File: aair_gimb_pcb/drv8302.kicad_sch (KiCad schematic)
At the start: 48 parts, among them U1 DRV8302, U3 TC2117

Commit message: pcb
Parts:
- D3: footprint Diode_SMD:D_SMA_Handsoldering -> Diode_SMD:D_SMA
- L1: footprint Inductor_SMD_Wurth:L_Wurth_WE-LQSH-2010 -> Inductor_SMD:L_7.3x7.3_H4.5
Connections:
- net GND: no longer C25.2, C26.2, C27.2, C31.1, C32.1, C33.1, C34.1, C35.1, C36.1, U1.29 (PVDD1)
- net H1_VS: now also R21.2
- net H2_VS: now also R22.2
- net H3_VS: now also R23.2
- net V_SUPPLY: now reaches C17.2, U1.53 (PVDD2), U1.54 (PVDD2)
- net V_SUPPLY: now also C25.2, C26.2, C27.2, C31.1, C32.1, C33.1, C34.1, C35.1, C36.1, U1.29 (PVDD1)
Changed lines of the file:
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@@
 	)
 	(junction
-		(at 85.09 69.85)
+		(at 162.56 68.58)
 		(diameter 0)
 		(color 0 0 0 0)
 	)
 	(junction
-		(at 157.48 144.78)
+		(at 85.09 69.85)
 		(diameter 0)
 		(color 0 0 0 0)
 	)
 	(junction
-		(at 158.75 129.54)
+		(at 157.48 144.78)
 		(diameter 0)
 		(color 0 0 0 0)
 	)
 	(junction
-		(at 177.8 68.58)
+		(at 158.75 129.54)
 		(diameter 0)
 		(color 0 0 0 0)
@@
 	)
 	(junction
-		(at 149.86 41.91)
-		(diameter 0)
-		(color 0 0 0 0)
-	)
-	(junction
 		(at 170.18 87.63)
 		(diameter 0)
@@
 	(wire
 		(pts
+			(xy 257.81 120.65) (xy 267.97 120.65)
+		)
+		(stroke
+			(width 0)
+			(type default)
+		)
+	)
+	(wire
+		(pts
 			(xy 85.09 69.85) (xy 110.49 69.85)
 		)
@@
 	(wire
 		(pts
-			(xy 154.94 68.58) (xy 166.37 68.58)
+			(xy 154.94 68.58) (xy 162.56 68.58)
 		)
 		(stroke
@@
 	(wire
 		(pts
+			(xy 162.56 60.96) (xy 162.56 68.58)
+		)
+		(stroke
+			(width 0)
+			(type default)
+		)
+	)
+	(wire
+		(pts
 			(xy 96.52 46.99) (xy 92.71 46.99)
 		)
@@
 	(wire
 		(pts
-			(xy 177.8 68.58) (xy 180.34 68.58)
+			(xy 171.45 68.58) (xy 180.34 68.58)
 		)
 		(stroke
@@
 	(wire
 		(pts
+			(xy 162.56 68.58) (xy 166.37 68.58)
+		)
+		(stroke
+			(width 0)
+			(type default)
+		)
+	)
+	(wire
+		(pts
 			(xy 83.82 129.54) (xy 83.82 140.97)
 		)
@@
 	(wire
 		(pts
-			(xy 90.17 26.67) (xy 90.17 30.48)
-		)
-		(stroke
-			(width 0)
-			(type default)
-		)
-	)
-	(wire
-		(pts
 			(xy 246.38 135.89) (xy 252.73 135.89)
 		)
@@
 	(wire
 		(pts
-			(xy 134.62 41.91) (xy 149.86 41.91)
-		)
-		(stroke
-			(width 0)
-			(type default)
-		)
-	)
-	(wire
-		(pts
 			(xy 96.52 44.45) (xy 121.92 44.45)
 		)
@@
 	(wire
 		(pts
-			(xy 149.86 41.91) (xy 149.86 43.18)
+			(xy 149.86 40.64) (xy 149.86 43.18)
 		)
 		(stroke
@@
 	(wire
 		(pts
+			(xy 177.8 60.96) (xy 162.56 60.96)
+		)
+		(stroke
+			(width 0)
+			(type default)
+		)
+	)
+	(wire
+		(pts
 			(xy 154.94 139.7) (xy 157.48 139.7)
 		)
@@
 	(wire
 		(pts
-			(xy 196.85 74.93) (xy 196.85 76.2)
+			(xy 269.24 132.08) (xy 257.81 132.08)
 		)
 		(stroke
@@
 	(wire
 		(pts
-			(xy 158.75 123.19) (xy 170.18 123.19)
+			(xy 196.85 74.93) (xy 196.85 76.2)
 		)
 		(stroke
@@
 	(wire
 		(pts
-			(xy 116.84 57.15) (xy 121.92 57.15)
+			(xy 158.75 123.19) (xy 170.18 123.19)
 		)
 		(stroke
@@
 	(wire
 		(pts
-			(xy 109.22 140.97) (xy 104.14 140.97)
+			(xy 116.84 57.15) (xy 121.92 57.15)
 		)
 		(stroke
@@
 	(wire
 		(pts
-			(xy 130.81 143.51) (xy 130.81 144.78)
+			(xy 109.22 140.97) (xy 104.14 140.97)
 		)
 		(stroke
@@
 	(wire
 		(pts
-			(xy 149.86 40.64) (xy 149.86 41.91)
+			(xy 130.81 143.51) (xy 130.81 144.78)
 		)
 		(stroke
@@
 	(wire
 		(pts
-			(xy 177.8 60.96) (xy 177.8 68.58)
+			(xy 257.81 107.95) (xy 267.97 107.95)
 		)
 		(stroke
@@
 	(wire
 		(pts
-			(xy 90.17 30.48) (xy 85.09 30.48)
-		)
-		(stroke
-			(width 0)
-			(type default)
-		)
-	)
-	(wire
-		(pts
 			(xy 92.71 46.99) (xy 92.71 54.61)
 		)
@@
 	(wire
 		(pts
-			(xy 171.45 68.58) (xy 177.8 68.58)
-		)
-		(stroke
-			(width 0)
-			(type default)
-		)
-	)
-	(wire
-		(pts
 			(xy 267.97 59.69) (xy 267.97 54.61)
 		)
@@
 	(global_label "V_SUPPLY"
 		(shape input)
-		(at 85.09 30.48 180)
-		(fields_autoplaced yes)
-		(effects
-			(font
-				(size 1.27 1.27)
-			)
-			(justify right)
-		)
-		(property "Intersheetrefs" "${INTERSHEET_REFS}"
-			(at 72.8519 30.48 0)
-			(effects
-				(font
-					(size 1.27 1.27)
-				)
-				(justify right)
-				(hide yes)
-			)
-		)
-	)
-	(global_label "V_SUPPLY"
-		(shape input)
 		(at 158.75 139.7 0)
 		(fields_autoplaced yes)
@@
 		)
 	)
+	(hierarchical_label "H2_VS"
+		(shape input)
+		(at 267.97 120.65 0)
+		(effects
+			(font
+				(size 1.27 1.27)
+			)
+			(justify left)
+		)
+	)
 	(hierarchical_label "DC_CAL"
 		(shape input)
@@
 		)
 	)
+	(hierarchical_label "H1_VS"
+		(shape input)
+		(at 267.97 107.95 0)
+		(effects
+			(font
+				(size 1.27 1.27)
+			)
+			(justify left)
+		)
+	)
 	(hierarchical_label "L1"
 		(shape input)
@@
 		)
 	)
+	(hierarchical_label "H3_VS"
+		(shape input)
+		(at 269.24 132.08 0)
+		(effects
+			(font
+				(size 1.27 1.27)
+			)
+			(justify left)
+		)
+	)
 	(hierarchical_label "H3_LOW"
 		(shape input)
@@
 	)
 	(symbol
-		(lib_id "power:PWR_FLAG")
-		(at 134.62 41.91 0)
-		(unit 1)
-		(exclude_from_sim no)
-		(in_bom yes)
-		(on_board yes)
-		(dnp no)
-		(fields_autoplaced yes)
-		(property "Reference" "#FLG02"
-			(at 134.62 40.005 0)
-			(effects
-				(font
-					(size 1.27 1.27)
-				)
-				(hide yes)
-			)
-		)
-		(property "Value" "PWR_FLAG"
-			(at 134.62 36.83 0)
-			(effects
-				(font
-					(size 1.27 1.27)
-				)
-			)
-		)
-		(property "Footprint" ""
-			(at 134.62 41.91 0)
-			(effects
-				(font
-					(size 1.27 1.27)
-				)
-				(hide yes)
-			)
-		)
-		(property "Datasheet" "~"
-			(at 134.62 41.91 0)
-			(effects
-				(font
-					(size 1.27 1.27)
-				)
-				(hide yes)
-			)
-		)
-		(property "Description" "Special symbol for telling ERC where power comes from"
-			(at 134.62 41.91 0)
-			(effects
-				(font
-					(size 1.27 1.27)
-				)
-				(hide yes)
-			)
-		)
-		(pin "1"
-		)
-		(instances
-			(project "aair_gimb_pcb"
-				(path "/d04c5395-2e3c-40b8-8677-11fb81ced555/526064b6-8a4a-401a-a09d-5ba18d5a28f8"
-					(reference "#FLG02")
-					(unit 1)
-				)
-			)
-		)
-	)
-	(symbol
 		(lib_id "Device:C_Small")
 		(at 168.91 68.58 270)
@@
 	)
 	(symbol
-		(lib_id "power:PWR_FLAG")
-		(at 90.17 26.67 0)
-		(unit 1)
-		(exclude_from_sim no)
-		(in_bom yes)
-		(on_board yes)
-		(dnp no)
-		(fields_autoplaced yes)
-		(property "Reference" "#FLG01"
-			(at 90.17 24.765 0)
-			(effects
-				(font
-					(size 1.27 1.27)
-				)
-				(hide yes)
-			)
-		)
-		(property "Value" "PWR_FLAG"
-			(at 90.17 21.59 0)
-			(effects
-				(font
-					(size 1.27 1.27)
-				)
-			)
-		)
-		(property "Footprint" ""
-			(at 90.17 26.67 0)
-			(effects
-				(font
-					(size 1.27 1.27)
-				)
-				(hide yes)
-			)
-		)
-		(property "Datasheet" "~"
-			(at 90.17 26.67 0)
-			(effects
-				(font
-					(size 1.27 1.27)
-				)
-				(hide yes)
-			)
-		)
-		(property "Description" "Special symbol for telling ERC where power comes from"
-			(at 90.17 26.67 0)
-			(effects
-				(font
-					(size 1.27 1.27)
-				)
-				(hide yes)
-			)
-		)
-		(pin "1"
-		)
-		(instances
-			(project ""
-				(path "/d04c5395-2e3c-40b8-8677-11fb81ced555/526064b6-8a4a-401a-a09d-5ba18d5a28f8"
-					(reference "#FLG01")
-					(unit 1)
-				)
-			)
-		)
-	)
-	(symbol
 		(lib_id "Device:C_Small")
 		(at 256.54 49.53 90)
@@
 			)
 		)
-		(property "Footprint" "Inductor_SMD_Wurth:L_Wurth_WE-LQSH-2010"
+		(property "Footprint" "Inductor_SMD:L_7.3x7.3_H4.5"
 			(at 203.2 74.93 0)
 			(effects
@@
 			)
 		)
-		(property "Footprint" "Diode_SMD:D_SMA_Handsoldering"
+		(property "Footprint" "Diode_SMD:D_SMA"
 			(at 196.85 80.01 0)
 			(effects

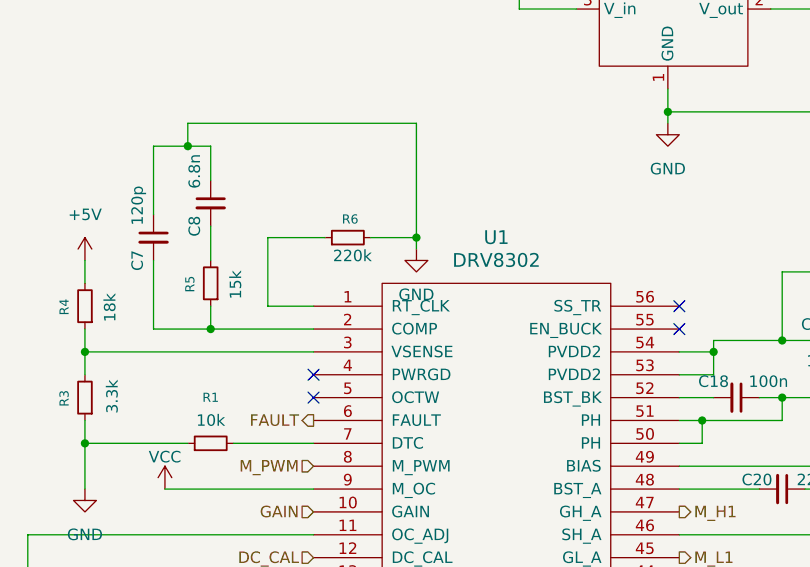
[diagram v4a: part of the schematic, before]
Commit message: add digital logic to pcb
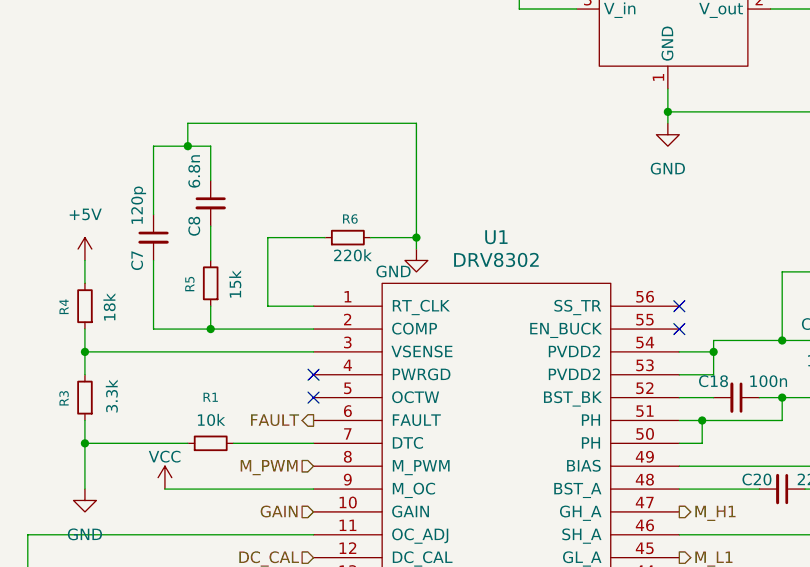
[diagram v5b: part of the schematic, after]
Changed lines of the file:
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@@
 		(on_board yes)
 		(dnp no)
-		(fields_autoplaced yes)
 		(property "Reference" "#PWR08"
 			(at 121.92 64.77 0)
@@
 		)
 		(property "Value" "GND"
-			(at 121.92 63.5 0)
+			(at 119.38 60.96 0)
 			(effects
 				(font

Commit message: fix exeption to pcb
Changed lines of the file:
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@@
 		(lib_id "Device:C_Small")
 		(at 104.14 135.89 0)
+		(mirror y)
 		(unit 1)
 		(exclude_from_sim no)
@@
 		(dnp no)
 		(property "Reference" "C2"
-			(at 102.362 138.43 90)
+			(at 105.918 138.43 90)
 			(effects
 				(font
@@
 		)
 		(property "Value" "2.2u"
-			(at 102.362 132.334 90)
+			(at 105.918 132.334 90)
 			(effects
 				(font

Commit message: done
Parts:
- U1: footprint CRF1:TSSOP-56-PP -> Package_SO:HTSSOP-56-1EP_6.1x14mm_P0.5mm_EP3.61x6.35mm
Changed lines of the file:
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@@
 			)
 		)
-		(property "Footprint" "CRF1:TSSOP-56-PP"
+		(property "Footprint" "Package_SO:HTSSOP-56-1EP_6.1x14mm_P0.5mm_EP3.61x6.35mm"
 			(at 130.81 99.06 0)
 			(effects
